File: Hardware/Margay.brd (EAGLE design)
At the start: 50.2 x 30.4 mm, 71 parts, among them IC1 ATMEGA644M, J1 CONN_42.54_SCREW, J2 CONN_6SCREW_2.54, Q1 FDN360P, Q2 DMG3404, Q3 2N7002, Q4 FDN360P, Q6 FDN360P, U2 FT231X-Q

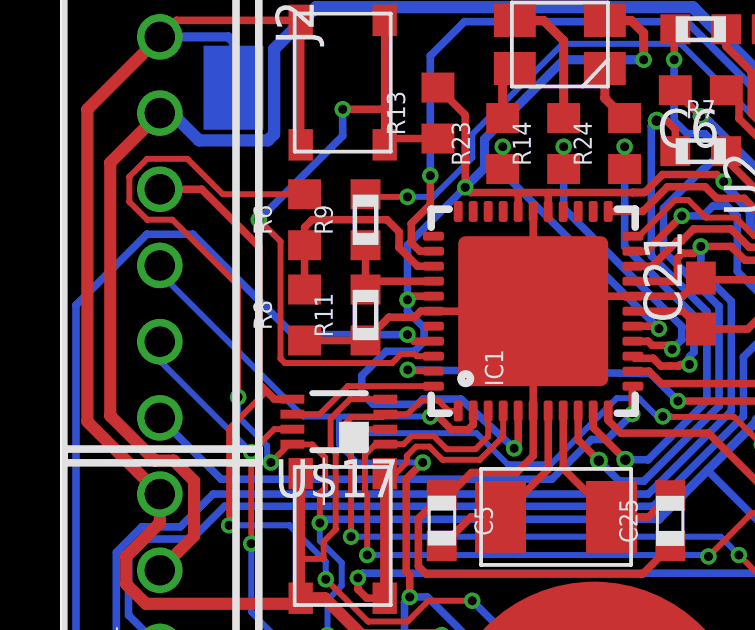
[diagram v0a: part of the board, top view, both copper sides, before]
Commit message: Updated test files, pick and place info, and fixed part info
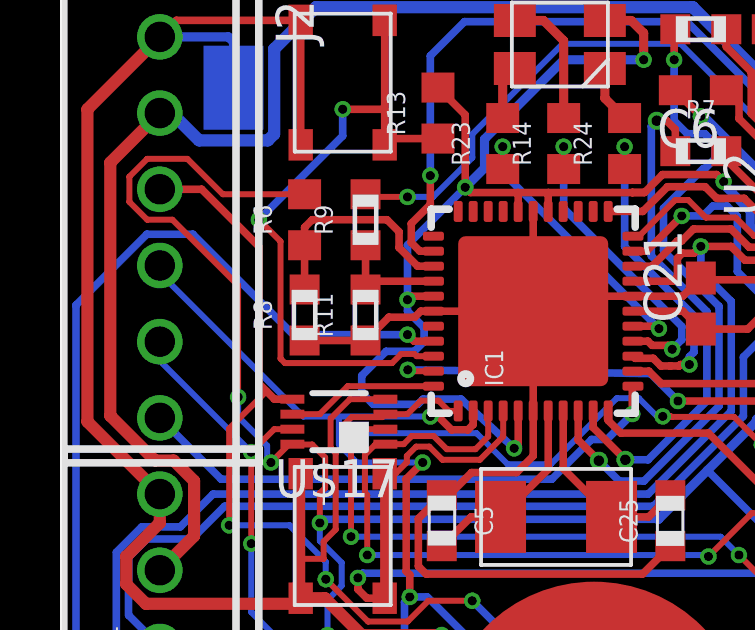
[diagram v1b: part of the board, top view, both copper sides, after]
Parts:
- R8: device bschulz:R0603 -> bschulz_passives:R0603
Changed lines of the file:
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@@
 </element>
 <element name="R1" library="bschulz_passives" package="R0603" value="10k" x="32.131" y="10.033" rot="R90">
-<attribute name="DIGIKEY" value="311-10.0KHRCT-ND" x="32.131" y="10.033" size="1.778" layer="27" rot="R90" display="off"/>
-<attribute name="MF" value="Yageo" x="32.131" y="10.033" size="1.778" layer="27" rot="R90" display="off"/>
-<attribute name="MPN" value="RC0603FR-0710KL" x="32.131" y="10.033" size="1.778" layer="27" rot="R90" display="off"/>
+<attribute name="DIGIKEY" value="P10.0KHCT-ND" x="32.131" y="10.033" size="1.778" layer="27" rot="R90" display="off"/>
+<attribute name="MF" value="Panasonic" x="32.131" y="10.033" size="1.778" layer="27" rot="R90" display="off"/>
+<attribute name="MPN" value="ERJ-3EKF1002V" x="32.131" y="10.033" size="1.778" layer="27" rot="R90" display="off"/>
 <attribute name="VALUE_PART" value="10k" x="32.131" y="10.033" size="1.778" layer="27" rot="R90" display="off"/>
 </element>
@@
 </element>
 <element name="R11" library="bschulz_passives" package="R0603" value="1.62M" x="10.16" y="19.558" rot="R90">
-<attribute name="DIGIKEY" value="RMCF0603FT1M62TR-ND" x="10.16" y="19.558" size="1.778" layer="27" rot="R90" display="off"/>
+<attribute name="DIGIKEY" value="RMCF0603FT1M62CT-ND" x="10.16" y="19.558" size="1.778" layer="27" rot="R90" display="off"/>
 <attribute name="MF" value="Stackpole" x="10.16" y="19.558" size="1.778" layer="27" rot="R90" display="off"/>
 <attribute name="MPN" value="RMCF0603FT1M62" x="10.16" y="19.558" size="1.778" layer="27" rot="R90" display="off"/>
@@
 </element>
 <element name="R12" library="bschulz_passives" package="R0603" value="10k" x="41.275" y="11.811">
-<attribute name="DIGIKEY" value="311-10.0KHRCT-ND" x="41.275" y="11.811" size="1.778" layer="27" display="off"/>
-<attribute name="MF" value="Yageo" x="41.275" y="11.811" size="1.778" layer="27" display="off"/>
-<attribute name="MPN" value="RC0603FR-0710KL" x="41.275" y="11.811" size="1.778" layer="27" display="off"/>
+<attribute name="DIGIKEY" value="P10.0KHCT-ND" x="41.275" y="11.811" size="1.778" layer="27" display="off"/>
+<attribute name="MF" value="Panasonic" x="41.275" y="11.811" size="1.778" layer="27" display="off"/>
+<attribute name="MPN" value="ERJ-3EKF1002V" x="41.275" y="11.811" size="1.778" layer="27" display="off"/>
 <attribute name="VALUE_PART" value="10k" x="41.275" y="11.811" size="1.778" layer="27" display="off"/>
 </element>
@@
 </element>
 <element name="R15" library="bschulz_passives" package="R0603" value="10k" x="8.509" y="1.397" rot="R180">
-<attribute name="DIGIKEY" value="311-10.0KHRCT-ND" x="8.509" y="1.397" size="1.778" layer="27" rot="R180" display="off"/>
-<attribute name="MF" value="Yageo" x="8.509" y="1.397" size="1.778" layer="27" rot="R180" display="off"/>
-<attribute name="MPN" value="RC0603FR-0710KL" x="8.509" y="1.397" size="1.778" layer="27" rot="R180" display="off"/>
+<attribute name="DIGIKEY" value="P10.0KHCT-ND" x="8.509" y="1.397" size="1.778" layer="27" rot="R180" display="off"/>
+<attribute name="MF" value="Panasonic" x="8.509" y="1.397" size="1.778" layer="27" rot="R180" display="off"/>
+<attribute name="MPN" value="ERJ-3EKF1002V" x="8.509" y="1.397" size="1.778" layer="27" rot="R180" display="off"/>
 <attribute name="VALUE_PART" value="10k" x="8.509" y="1.397" size="1.778" layer="27" rot="R180" display="off"/>
 </element>
@@
 <attribute name="VALUE_PART" value="330" x="21.336" y="25.019" size="1.778" layer="27" display="off"/>
 </element>
-<element name="R8" library="bschulz" package="R0603" value="" x="8.128" y="19.558" rot="R90">
+<element name="R8" library="bschulz_passives" package="R0603" value="" x="8.128" y="19.558" rot="R90">
 <attribute name="DIGIKEY" value="P10KDBCT-ND " x="8.128" y="19.558" size="1.778" layer="27" rot="R90" display="off"/>
 <attribute name="MF" value="Panasonic" x="8.128" y="19.558" size="1.778" layer="27" rot="R90" display="off"/>
 <attribute name="MPN" value="ERA-3AEB103V" x="8.128" y="19.558" size="1.778" layer="27" rot="R90" display="off"/>
-<attribute name="VALUE_PART" value="" x="8.128" y="19.558" size="1.778" layer="27" rot="R90" display="off"/>
+<attribute name="VALUE_PART" value="10k" x="8.128" y="19.558" size="1.778" layer="27" rot="R90" display="off"/>
 </element>
 <element name="R9" library="bschulz_passives" package="R0603" value="1.62M" x="10.16" y="22.733" rot="R90">
-<attribute name="DIGIKEY" value="RMCF0603FT1M62TR-ND" x="10.16" y="22.733" size="1.778" layer="27" rot="R90" display="off"/>
+<attribute name="DIGIKEY" value="RMCF0603FT1M62CT-ND" x="10.16" y="22.733" size="1.778" layer="27" rot="R90" display="off"/>
 <attribute name="MF" value="Stackpole" x="10.16" y="22.733" size="1.778" layer="27" rot="R90" display="off"/>
 <attribute name="MPN" value="RMCF0603FT1M62" x="10.16" y="22.733" size="1.778" layer="27" rot="R90" display="off"/>
@@
 </element>
 <element name="R17" library="bschulz_passives" package="R0603" value="10k" x="39.497" y="19.304" rot="R90">
-<attribute name="DIGIKEY" value="311-10.0KHRCT-ND" x="39.497" y="19.304" size="1.778" layer="27" rot="R90" display="off"/>
-<attribute name="MF" value="Yageo" x="39.497" y="19.304" size="1.778" layer="27" rot="R90" display="off"/>
-<attribute name="MPN" value="RC0603FR-0710KL" x="39.497" y="19.304" size="1.778" layer="27" rot="R90" display="off"/>
+<attribute name="DIGIKEY" value="P10.0KHCT-ND" x="39.497" y="19.304" size="1.778" layer="27" rot="R90" display="off"/>
+<attribute name="MF" value="Panasonic" x="39.497" y="19.304" size="1.778" layer="27" rot="R90" display="off"/>
+<attribute name="MPN" value="ERJ-3EKF1002V" x="39.497" y="19.304" size="1.778" layer="27" rot="R90" display="off"/>
 <attribute name="VALUE_PART" value="10k" x="39.497" y="19.304" size="1.778" layer="27" rot="R90" display="off"/>
 </element>

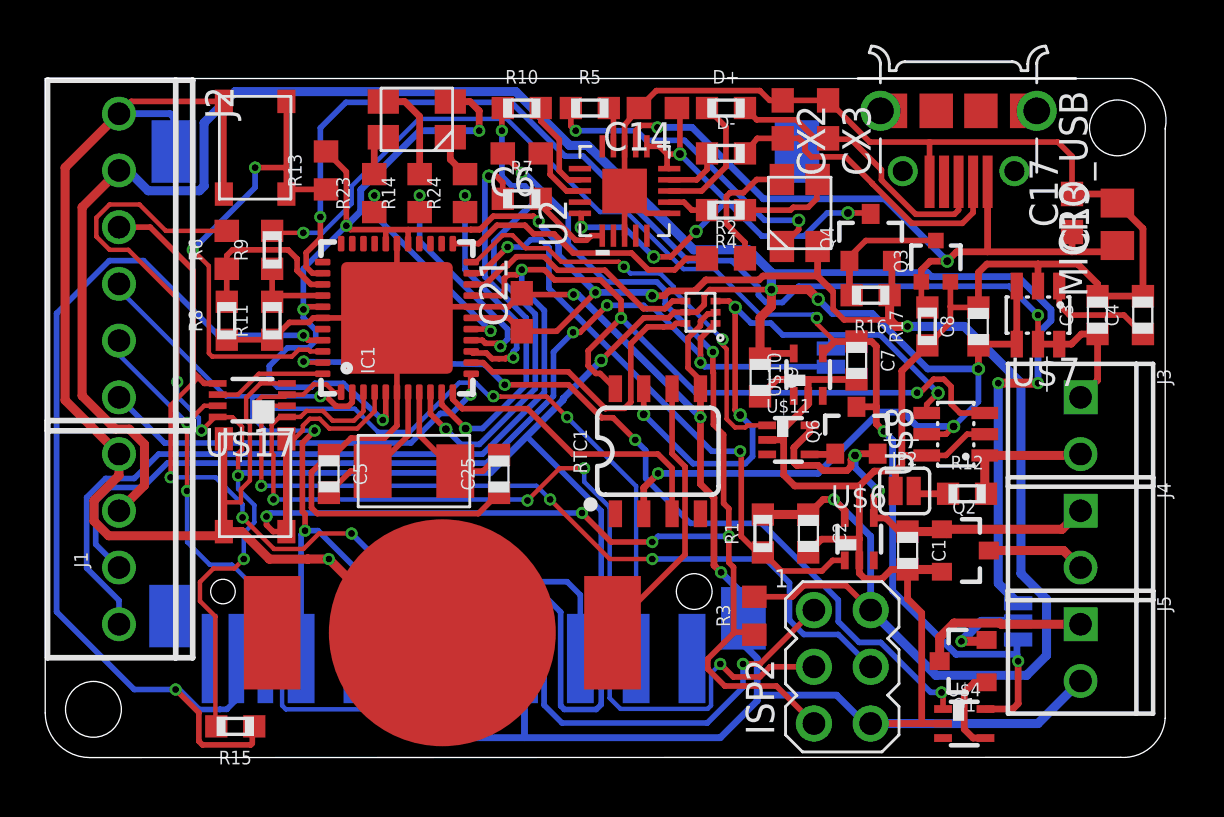
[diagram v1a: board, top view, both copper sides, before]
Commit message: Added reference designators and legacy hardware test
Added legacy hardware testing file and reference designator image
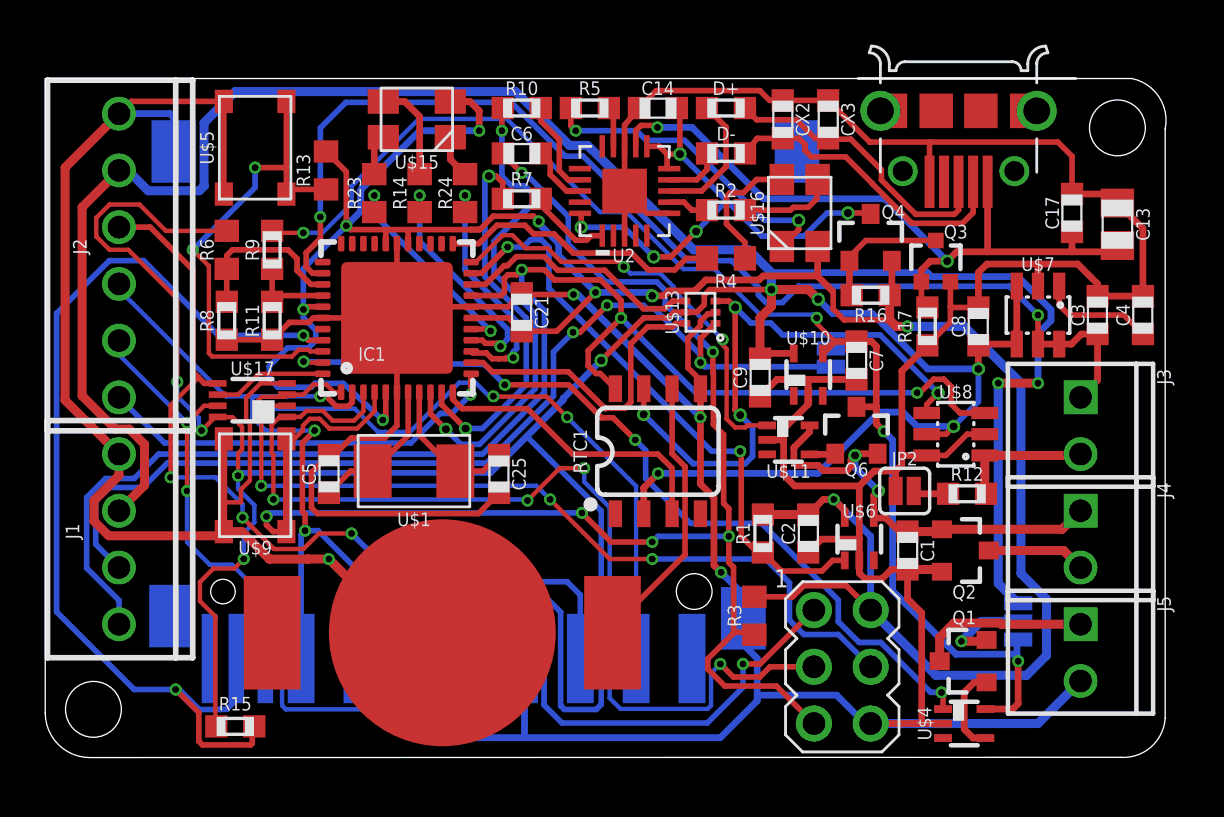
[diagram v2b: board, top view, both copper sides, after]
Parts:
- C13: device bschulz:C0805 -> bschulz_passives:C0805
- C14, C17, C21, C6, CX2, CX3: device bschulz:C0603 -> bschulz_passives:C0603

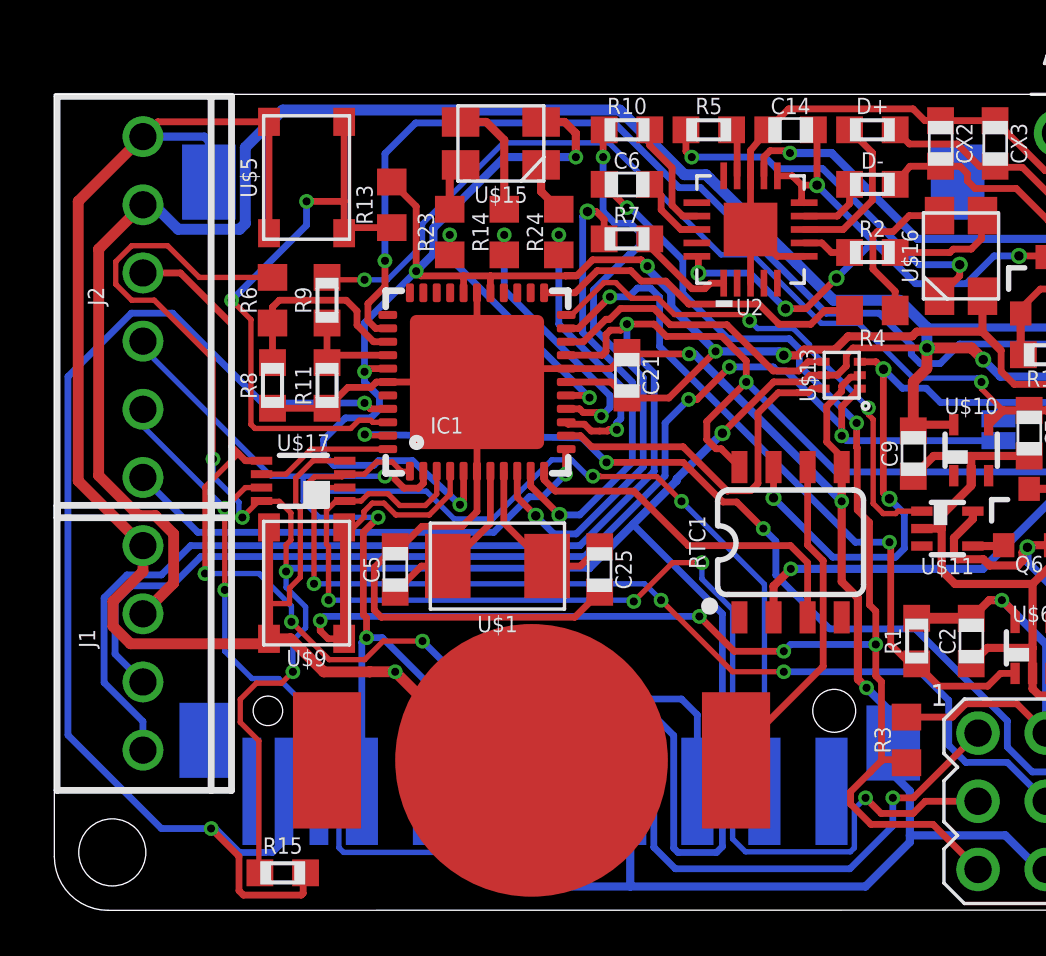
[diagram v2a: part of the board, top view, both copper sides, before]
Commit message: Fixed button layout (#14)
Updated button layout from Cold Silicon updates, fixed resulting layout issues
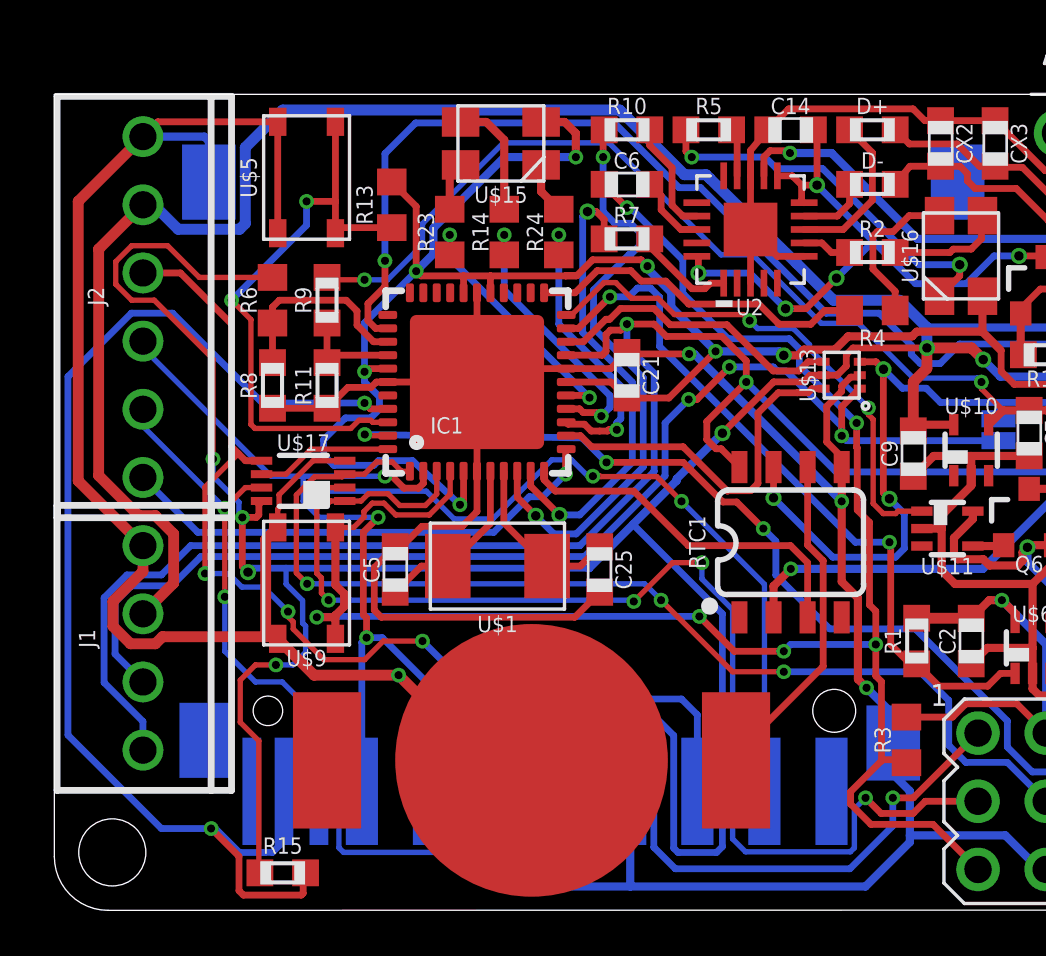
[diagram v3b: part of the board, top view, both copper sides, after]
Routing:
- net GND: track 282.6 -> 279.4 mm
- net 3V3_AUX: track 216.9 -> 217.8 mm
- net SCK: track 45.7 -> 46.3 mm

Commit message: Cleaned up schematic, added board and schematic images for v1.0
Added documentation for version 1.0, added schematic PDF, board images, and updated BOM to fix ADC part number
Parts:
- D+, D-: value 27ohm -> 27
- U$8: value MCP3425 -> MCP3421A1
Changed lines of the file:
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@@
 <attribute name="VALUE" x="33.655" y="28.575" size="0.6096" layer="27" font="vector" ratio="15" rot="R270" align="center"/>
 </element>
-<element name="D+" library="bschulz_passives" package="R0603" value="27ohm" x="30.48" y="29.083" smashed="yes">
+<element name="D+" library="bschulz_passives" package="R0603" value="27" x="30.48" y="29.083" smashed="yes">
 <attribute name="DIGIKEY" value="311-27.0HRCT-ND" x="30.48" y="29.083" size="1.778" layer="27" display="off"/>
 <attribute name="MF" value="Yageo" x="30.48" y="29.083" size="1.778" layer="27" display="off"/>
@@
 <attribute name="VALUE_PART" value="27" x="30.48" y="29.083" size="1.778" layer="27" display="off"/>
 </element>
-<element name="D-" library="bschulz_passives" package="R0603" value="27ohm" x="30.48" y="27.051" smashed="yes">
+<element name="D-" library="bschulz_passives" package="R0603" value="27" x="30.48" y="27.051" smashed="yes">
 <attribute name="DIGIKEY" value="311-27.0HRCT-ND" x="30.48" y="27.051" size="1.778" layer="27" display="off"/>
 <attribute name="MF" value="Yageo" x="30.48" y="27.051" size="1.778" layer="27" display="off"/>
@@
 <attribute name="VALUE" x="44.45" y="22.225" size="0.6096" layer="27" font="vector" ratio="15" rot="R180" align="center"/>
 </element>
-<element name="U$8" library="bschulz" package="SOT23-6L" value="MCP3425" x="40.767" y="14.478" smashed="yes" rot="R90">
-<attribute name="DIGIKEY" value="MCP3425A0T-E/CHCT-ND" x="40.767" y="14.478" size="1.778" layer="27" rot="R90" display="off"/>
+<element name="U$8" library="bschulz" package="SOT23-6L" value="MCP3421A1" x="40.767" y="14.478" smashed="yes" rot="R90">
+<attribute name="DIGIKEY" value="MCP3421A1T-E/CHCT-ND" x="40.767" y="14.478" size="1.778" layer="27" rot="R90" display="off"/>
+<attribute name="DISP" value="MCP3421" x="40.767" y="14.478" size="1.778" layer="27" rot="R90" display="off"/>
 <attribute name="MF" value="Microchip" x="40.767" y="14.478" size="1.778" layer="27" rot="R90" display="off"/>
-<attribute name="MPN" value="MCP3425A0T-E/CH" x="40.767" y="14.478" size="1.778" layer="27" rot="R90" display="off"/>
+<attribute name="MPN" value="MCP3421A1T-E/CH" x="40.767" y="14.478" size="1.778" layer="27" rot="R90" display="off"/>
 <attribute name="NAME" x="40.767" y="16.383" size="0.6096" layer="25" font="vector" ratio="15" rot="R180" align="center"/>
 <attribute name="VALUE" x="43.18" y="14.478" size="0.6096" layer="27" font="vector" ratio="15" rot="R90" align="center"/>
